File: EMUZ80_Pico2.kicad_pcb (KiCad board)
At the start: 2 copper layers, 99.1 x 82.5 mm, 12 parts, among them J1 Conn_01x20_Socket, J2 Conn_01x20_Socket, J7 Conn_01x02_Pin

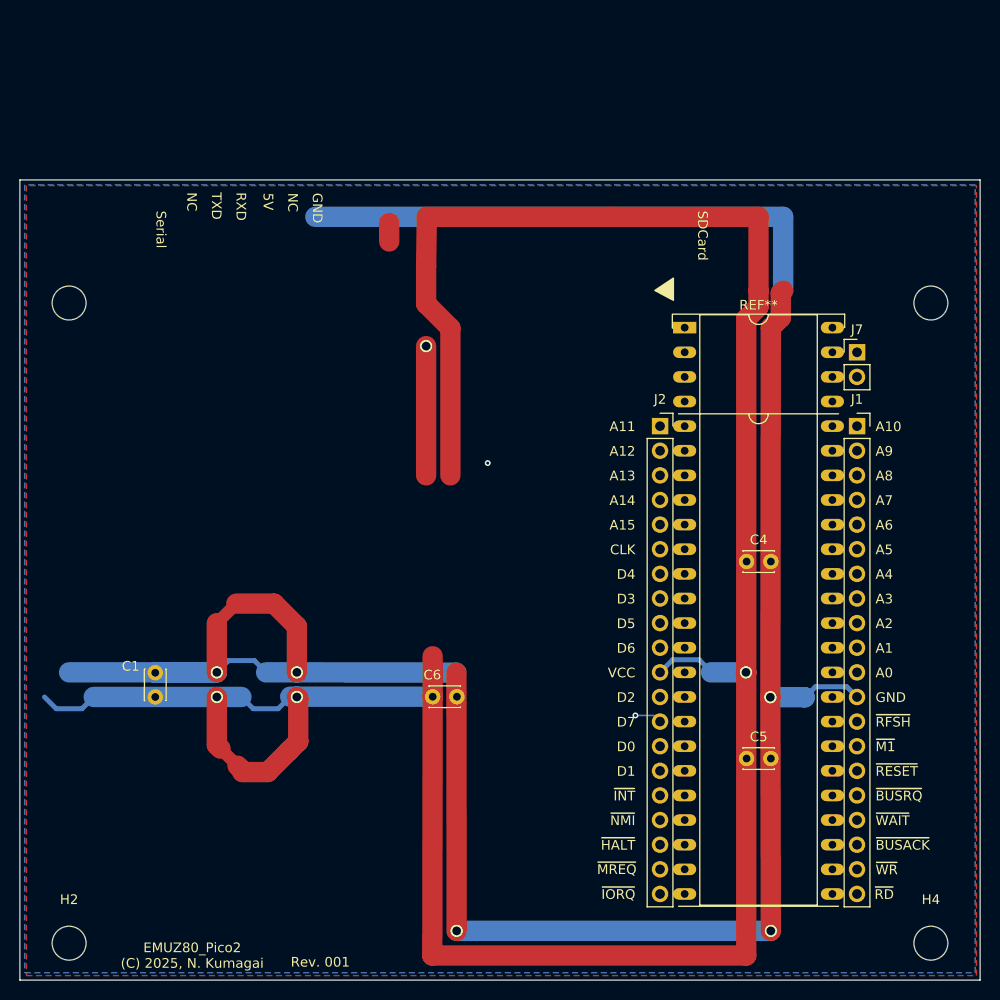
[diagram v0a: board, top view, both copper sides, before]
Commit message: schematic done, pcb now working
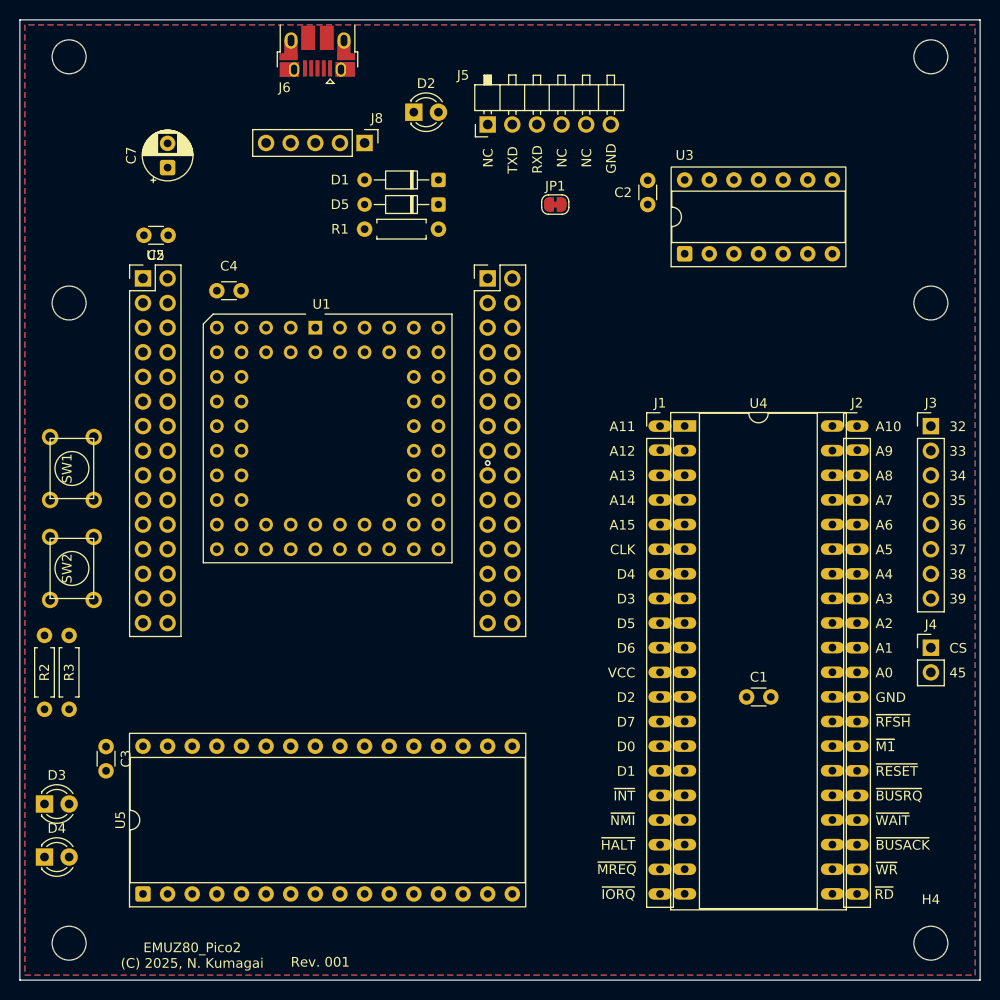
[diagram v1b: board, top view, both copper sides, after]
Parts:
- removed C6: 0.1uF, Capacitor_THT:C_Disc_D3.0mm_W2.0mm_P2.50mm
- removed J7: Conn_01x02_Pin, Connector_PinHeader_2.54mm:PinHeader_1x02_P2.54mm_Vertical
- removed REF**: DIP-48_W15.24mm_Socket_OvalPad_nocourtyard, 0-local:DIP-48_W15.24mm_Socket_OvalPad_splitcouryard
- added C2: 0.1u, Capacitor_THT:C_Disc_D3.0mm_W1.6mm_P2.50mm, F.Cu at (168.2, 58.5)
- added C3: 0.1u, Capacitor_THT:C_Disc_D3.0mm_W1.6mm_P2.50mm, F.Cu at (112.3, 116.9)
- added C7: 10uF, Capacitor_THT:CP_Radial_D5.0mm_P2.50mm, F.Cu at (118.6, 57.2)
- added D1: 1S3, local-f:D_DO-34_SOD68_P7.62mm_Horizontal, F.Cu at (146.6, 58.5)
- added D2: RED, local-f:LED_D3.0mm, F.Cu at (144.0, 51.5)
- added D3: GREEN, local-f:LED_D3.0mm, F.Cu at (105.9, 122.8)
- added D4: YELLOW, local-f:LED_D3.0mm, F.Cu at (105.9, 128.3)
- added D5: 1S3, local-f:D_DO-34_SOD68_P7.62mm_Horizontal, F.Cu at (146.6, 61.0)
- added H5: MountingHole, MountingHole:MountingHole_3.5mm, F.Cu at (197.4, 45.8)
- added H5: MountingHole, MountingHole:MountingHole_3.5mm, F.Cu at (108.5, 45.8)
- added J3: EXT_GPIO1, Connector_PinHeader_2.54mm:PinHeader_1x08_P2.54mm_Vertical, F.Cu at (197.4, 83.8)
- added J4: EXT_GPIO2, Connector_PinHeader_2.54mm:PinHeader_1x02_P2.54mm_Vertical, F.Cu at (197.4, 106.7)
- added J5: Serial, local-f:PinHeader_1x06_P2.54mm_Horizontal_NoFeet, F.Cu at (151.6, 52.7)
- added J6: USB_B_Micro, Connector_USB:USB_Micro-B_Amphenol_10103594-0001LF_Horizontal, F.Cu at (134.1, 45.2)
- added J8: Conn_01x05_Pin, Connector_PinHeader_2.54mm:PinHeader_1x05_P2.54mm_Vertical, F.Cu at (138.9, 54.6)
- added JP1: VCC_Jumper, Jumper:SolderJumper-2_P1.3mm_Bridged_RoundedPad1.0x1.5mm, F.Cu at (158.6, 61.0)
- added R1: 1k, local-f:R_Axial_L5.5mm_D2.0mm_P7.62mm_Horizontal, F.Cu at (146.6, 63.5)
- added R2: 1k, local-f:R_Axial_L5.5mm_D2.0mm_P7.62mm_Horizontal, F.Cu at (105.9, 113.1)
- added R3: 1k, local-f:R_Axial_L5.5mm_D2.0mm_P7.62mm_Horizontal, F.Cu at (108.5, 113.1)
- added SW1: RUN, local-f:Tact_SW, F.Cu at (108.8, 88.2)
- added SW2: BOOTSEL, local-f:Tact_SW, F.Cu at (108.8, 98.5)
- added U1: Pimoroni PGA2350B, local-f:PLCC-64_THT-Socket, F.Cu at (135.1, 85.1)
- added U2: RB2350B_Core_Board, local-f:RB2350B_Core_Board, F.Cu at (135.1, 86.4)
- added U3: 74HC00, Package_DIP:DIP-14_W7.62mm_Socket, F.Cu at (172.0, 66.1)
- added U4: Z80CPU, local-f:DIP-40_W15.24mm_Socket_OvalPad_splitcouryard, F.Cu at (172.0, 83.8)
- added U5: HM628128, Package_DIP:DIP-32_W15.24mm_Socket, F.Cu at (116.1, 132.1)
- C1, C4, C5: value 0.1uF -> 0.1u; footprint Capacitor_THT:C_Disc_D3.0mm_W2.0mm_P2.50mm -> Capacitor_THT:C_Disc_D3.0mm_W1.6mm_P2.50mm
- J1: value Conn_01x20_Socket -> Z80_L; footprint Connector_PinSocket_2.54mm:PinSocket_1x20_P2.54mm_Vertical -> local-f:PinHeader_1x20_P2.54mm_Ovalpad_Vertical
- J2: value Conn_01x20_Socket -> Z80_R; footprint Connector_PinSocket_2.54mm:PinSocket_1x20_P2.54mm_Vertical -> local-f:PinHeader_1x20_P2.54mm_Ovalpad_Vertical
- moved C5 80.5 mm to (118.7, 64.2), turned to 180 degrees
- moved C1 61.0 mm to (178.4, 111.8), turned to 0 degrees
- moved C4 59.2 mm to (126.2, 69.9), turned to 180 degrees
- moved J1 20.3 mm to (169.4, 83.8)
- moved J2 20.3 mm to (189.7, 83.8)
- renumbered H5 to H6
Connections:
- C1 pad 1: VCC -> /VCC
- C4 pad 1: VCC -> +5V
- C5 pad 1: VCC -> +5V
- J1 pad 1: /A10 -> A11
- J1 pad 10: /A1 -> D6
- J1 pad 11: /A0 -> /VCC
- J1 pad 12: GND -> D2
- J1 pad 13: /~{RFSH} -> D7
- J1 pad 14: /~{M1} -> D0
- J1 pad 15: /~{RESET} -> D1
- J1 pad 16: /~{BUSRQ} -> INT
- J1 pad 17: /~{WAIT} -> NMI
- J1 pad 18: /~{BUSAK} -> HALT
- J1 pad 19: /~{WR} -> MREQ
- J1 pad 2: /A9 -> A12
- J1 pad 20: /~{RD} -> IORQ
- J1 pad 3: /A8 -> A13
- J1 pad 4: /A7 -> A14
- J1 pad 5: /A6 -> A15
- J1 pad 6: /A5 -> CLK
- J1 pad 7: /A4 -> D4
- J1 pad 8: /A3 -> D3
- J1 pad 9: /A2 -> D5
- J2 pad 1: /A11 -> A10
- J2 pad 10: /D6 -> A1
- J2 pad 11: VCC -> A0
- J2 pad 12: /D2 -> GND
- J2 pad 13: /D7 -> RFSH
- J2 pad 14: /D0 -> M1
- J2 pad 15: /D1 -> RESET
- J2 pad 16: /~{INT} -> BUSRQ
- J2 pad 17: /~{NMI} -> WAIT
- J2 pad 18: /~{HALT} -> BUSAK
- J2 pad 19: /~{MREQ} -> WR
- J2 pad 2: /A12 -> A9
- J2 pad 20: /~{IORQ} -> RD
- J2 pad 3: /A13 -> A8
- J2 pad 4: /A14 -> A7
- J2 pad 5: /A15 -> A6
- J2 pad 6: /CLK -> A5
- J2 pad 7: /D4 -> A4
- J2 pad 8: /D3 -> A3
- J2 pad 9: /D5 -> A2
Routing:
- net VCC: track 274.8 -> 0.00 mm, vias 3 -> 0
- net GND: track 271.9 -> 0.00 mm, vias 7 -> 0
- net /D7: track 2.80 -> 0.00 mm, vias 1 -> 0
- net Net-(SW1-C): track 1.90 -> 0.00 mm
- net /GPIO41: vias 0 -> 1
- added copper zone on F.Cu, net (none)
- removed copper zone on F.Cu, net VCC
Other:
- board size 99.1 x 82.5 mm -> 99.1 x 99.1 mm
- board text added: "32"
- board text added: "33"
- board text added: "34"
- board text added: "35"
- board text added: "36"
- board text added: "37"
- board text added: "38"
- board text added: "39"
- board text added: "45"
- board text added: "CS"
- board text removed: "5V"
- board text removed: "SDCard"
- board text removed: "Serial"

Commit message: EMUZ80_Pico2: PCB routing completed, ready to order
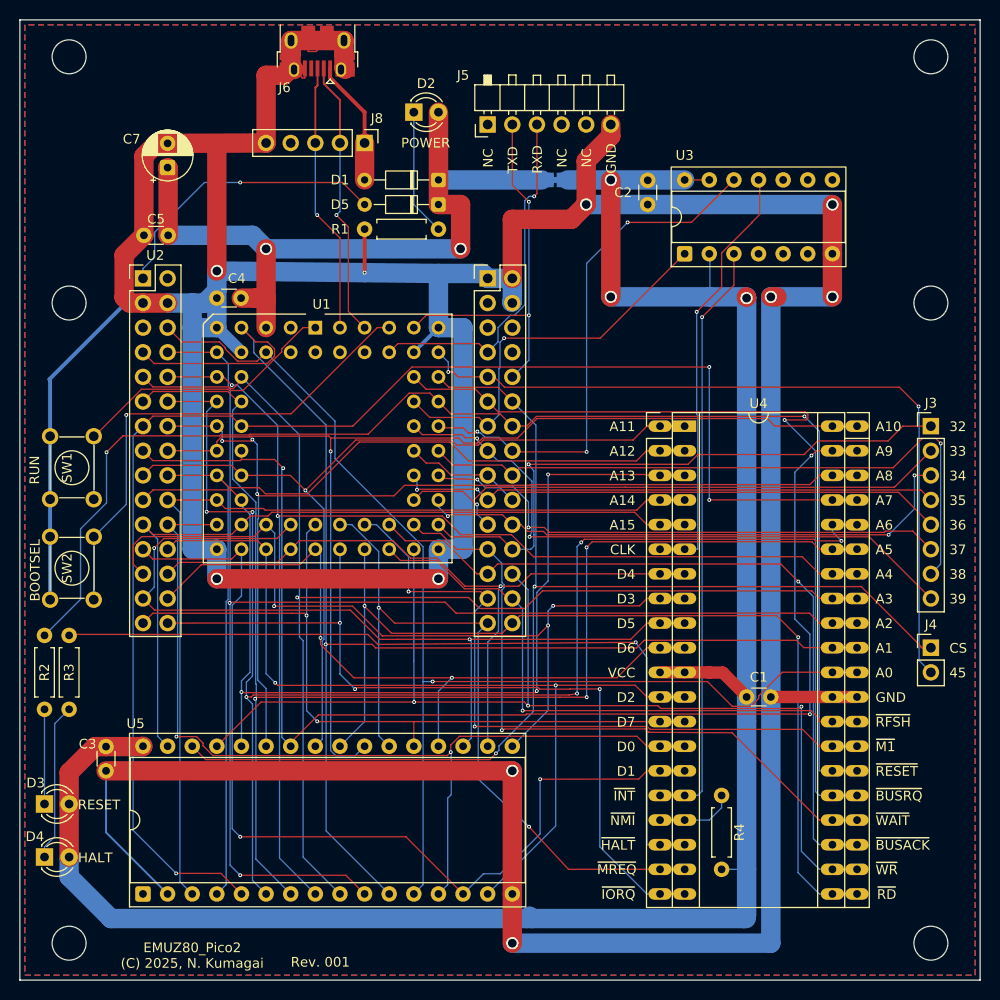
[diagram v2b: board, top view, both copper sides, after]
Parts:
- removed J1: Z80_L, local-f:PinHeader_1x20_P2.54mm_Ovalpad_Vertical
- removed J2: Z80_R, local-f:PinHeader_1x20_P2.54mm_Ovalpad_Vertical
- added R4: 10k, local-f:R_Axial_L5.5mm_D2.0mm_P7.62mm_Horizontal, F.Cu at (175.8, 129.6)
- JP1: moved to B.Cu
- U4: footprint local-f:DIP-40_W15.24mm_Socket_OvalPad_splitcouryard -> local-f:DIP-40_SidePin_Z80
- moved JP1 2.54 mm to (158.6, 58.5)
- moved C4 0.76 mm to (126.2, 70.6)
- moved SW1 0.08 mm to (108.8, 88.1)
- renumbered H2 to H1, H4 to H2, H6 to H3, H6 to H4, H5 to H6
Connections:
- net /VCC renamed Net-(D3-A)
- C3 pad 2: unconnected-(C3-Pad2) -> GND
- U4 pad 17: NMI -> Net-(U4-~{NMI})
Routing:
- net GND: track 0.00 -> 504.8 mm, vias 0 -> 10
- net Net-(D3-A): track 0.00 -> 234.1 mm, vias 0 -> 3
- net A7: track 0.00 -> 146.8 mm, vias 0 -> 3
- net A6: track 0.00 -> 143.8 mm, vias 0 -> 6
- net A5: track 0.00 -> 143.1 mm, vias 0 -> 3
- net A1: track 0.00 -> 139.8 mm, vias 0 -> 1
- net A2: track 0.00 -> 139.4 mm, vias 0 -> 2
- net RESET: track 0.00 -> 139.0 mm, vias 0 -> 2
- net A9: track 0.24 -> 133.4 mm, vias 0 -> 3
- net A3: track 0.00 -> 128.4 mm, vias 0 -> 1
- net A4: track 0.00 -> 125.6 mm, vias 0 -> 2
- net RAMCS: track 0.00 -> 123.4 mm, vias 0 -> 2
- net A0: track 0.00 -> 122.5 mm, vias 0 -> 1
- net WR: track 0.00 -> 114.0 mm, vias 0 -> 3
- net A10: track 0.00 -> 110.3 mm, vias 0 -> 1
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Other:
- board text added: "BOOTSEL"
- board text added: "HALT"
- board text added: "POWER"
- board text added: "RESET"
- board text added: "RUN"

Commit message: PCB rev001 finished, ready to order JLCPCB
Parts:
- U5: footprint Package_DIP:DIP-32_W15.24mm_Socket -> local-f:DIP-32_W15.24mm_OvalPads
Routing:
- net A9: track 133.4 -> 109.7 mm, vias 3 -> 1
- net A15: track 81.7 -> 104.5 mm, vias 0 -> 2
- net A12: track 101.7 -> 124.0 mm, vias 0 -> 4
- net A8: track 105.1 -> 124.9 mm, vias 3 -> 5
- net A13: track 104.7 -> 85.1 mm, vias 3 -> 2
- net A5: track 143.1 -> 123.6 mm, vias 3 -> 1
- net A14: track 95.9 -> 115.0 mm, vias 0 -> 4
- net A2: track 139.4 -> 121.5 mm, vias 2 -> 1
- net Net-(D3-A): track 234.1 -> 216.8 mm
- net RESET: track 139.0 -> 153.5 mm, vias 2 -> 5
- net GPIO38: track 68.6 -> 57.8 mm, vias 1 -> 2
- net RAMCS: track 123.4 -> 133.3 mm
- net D3: track 86.9 -> 96.8 mm, vias 3 -> 2
- net D4: track 75.6 -> 84.4 mm, vias 1 -> 3
- net D5: track 90.5 -> 99.0 mm, vias 2 -> 4
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
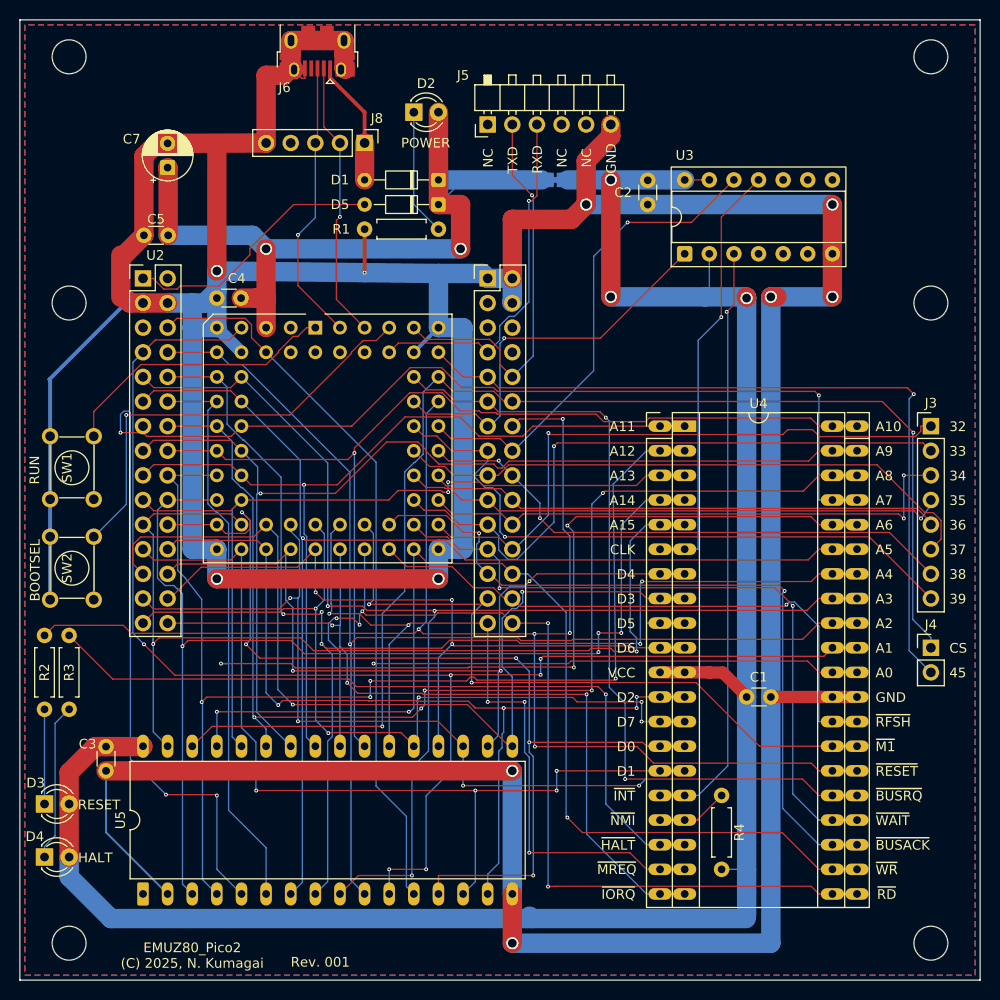
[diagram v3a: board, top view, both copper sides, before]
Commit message: add JP2-5 to SRAM Controls
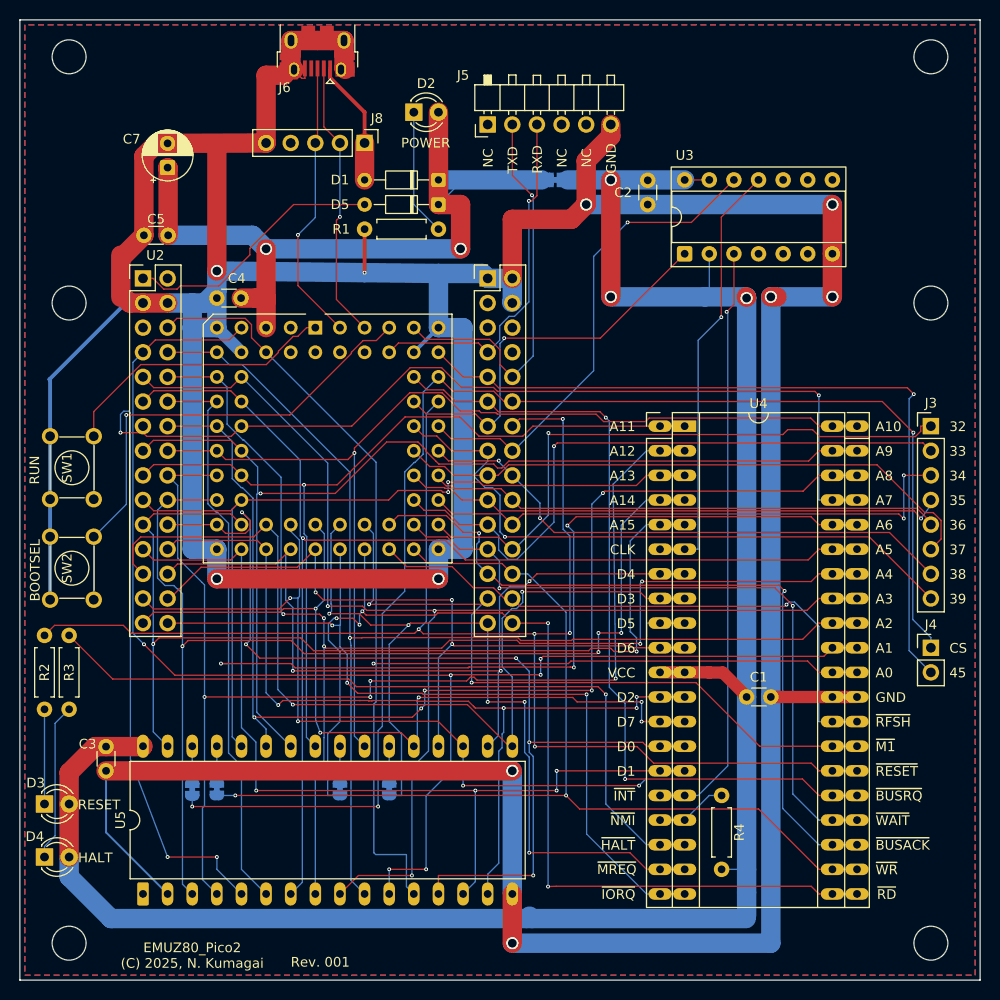
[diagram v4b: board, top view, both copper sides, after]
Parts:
- added JP2: CE1_J, Jumper:SolderJumper-2_P1.3mm_Bridged_RoundedPad1.0x1.5mm, B.Cu at (141.5, 121.3)
- added JP3: CS2_J, Jumper:SolderJumper-2_P1.3mm_Bridged_RoundedPad1.0x1.5mm, B.Cu at (121.2, 121.3)
- added JP4: OE_J, Jumper:SolderJumper-2_P1.3mm_Bridged_RoundedPad1.0x1.5mm, B.Cu at (136.4, 121.3)
- added JP5: WE_J, Jumper:SolderJumper-2_P1.3mm_Bridged_RoundedPad1.0x1.5mm, B.Cu at (123.7, 121.3)
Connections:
- U5 pad 22: MREQ -> Net-(JP2-A)
- U5 pad 24: RD -> Net-(JP4-A)
- U5 pad 29: WR -> Net-(JP5-A)
- U5 pad 30: RAMCS -> Net-(JP3-A)
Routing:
- net RAMCS: track 133.3 -> 141.4 mm, vias 2 -> 3
- net RD: track 104.3 -> 111.1 mm
- net MREQ: track 84.4 -> 91.2 mm
- net WR: track 112.1 -> 106.5 mm, vias 3 -> 2
- net Net-(JP3-A): track 0.00 -> 3.81 mm
- net Net-(JP5-A): track 0.00 -> 3.53 mm
- net Net-(JP4-A): track 0.00 -> 3.53 mm
- net Net-(JP2-A): track 0.00 -> 3.53 mm
- net A0: track 125.7 -> 127.8 mm
- net A4: track 129.4 -> 127.8 mm
- net A7: track 152.2 -> 151.3 mm
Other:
- board text added: "CS2"
- board text added: "~{CS1}"
- board text added: "~{OE}"
- board text added: "~{WE}"

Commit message: Rev001: order data
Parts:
- J6: footprint Connector_USB:USB_Micro-B_Amphenol_10103594-0001LF_Horizontal -> local-f:USB_Micro-B_Hirose_ZX62-B-5PA
- moved J6 1.02 mm to (134.1, 44.2), turned to 0 degrees
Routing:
- net GND: track 501.1 -> 497.6 mm
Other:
- board text added: "D+"
- board text added: "D-"
- board text added: "ID"
- board text added: "VBUS"
